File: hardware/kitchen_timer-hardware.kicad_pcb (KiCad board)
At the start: 2 copper layers, 60 x 110.8 mm, 80 parts, among them J1 Conn_01x02, J2 Conn_01x02_Pin, J3 AVR-ISP-6, Q1 JSM2302, Q2 IRLML6402, Q3 MMBT3904, SW2 SKRPACE010, U1 CH340E UART Module, U10 MAX7219, U11 KWM-20882CUYB, U12 KWM-20882CUYB, U13 KWM-20882CUYB, U14 KWM-20882CUYB, U2 TP4056 breakout, U3 SparkFun_LiPower, U5 ATMEGA328P-AU, U6 PEC11R-4215F-S0024, U7 MAX7219, U8 MAX7219, U9 MAX7219, Y1 Crystal-32kHz

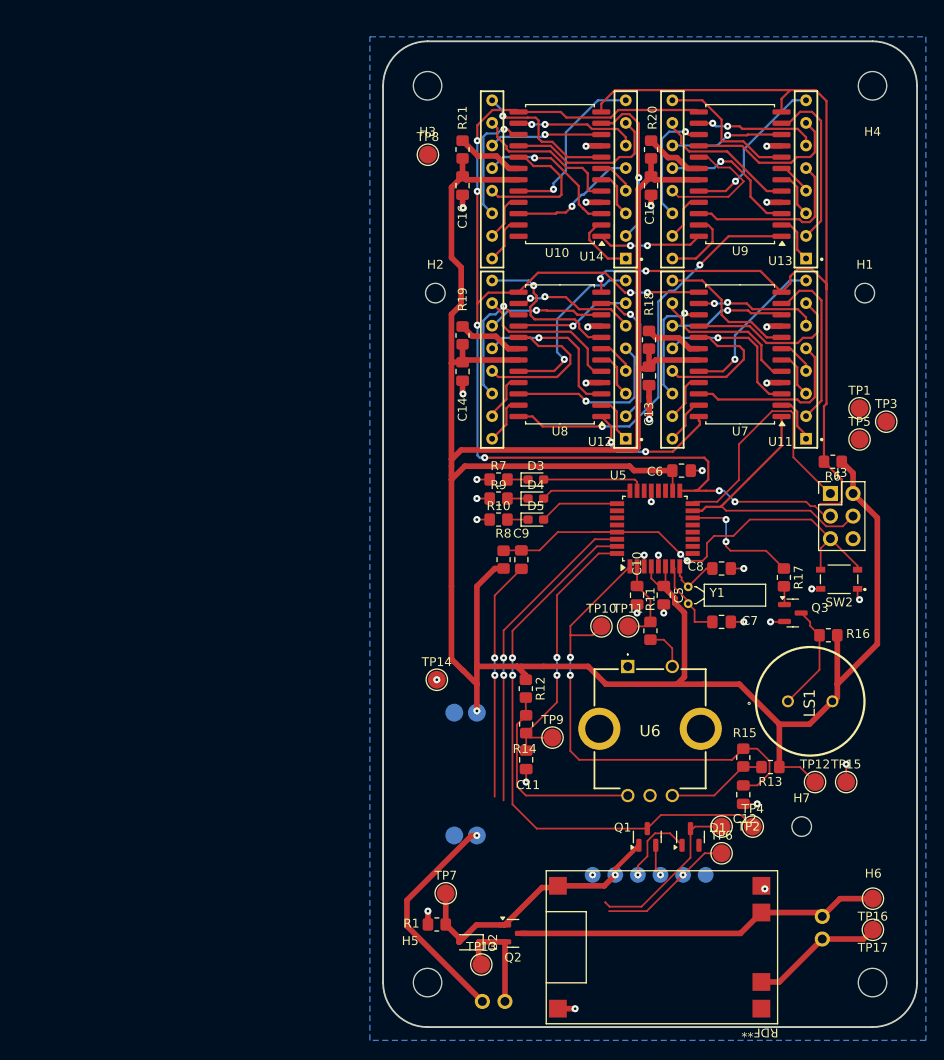
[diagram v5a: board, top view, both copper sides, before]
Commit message: Search/replace via size to adhere to JLCPCB fabrication rules
Down from 130 to 85 DRC rules now
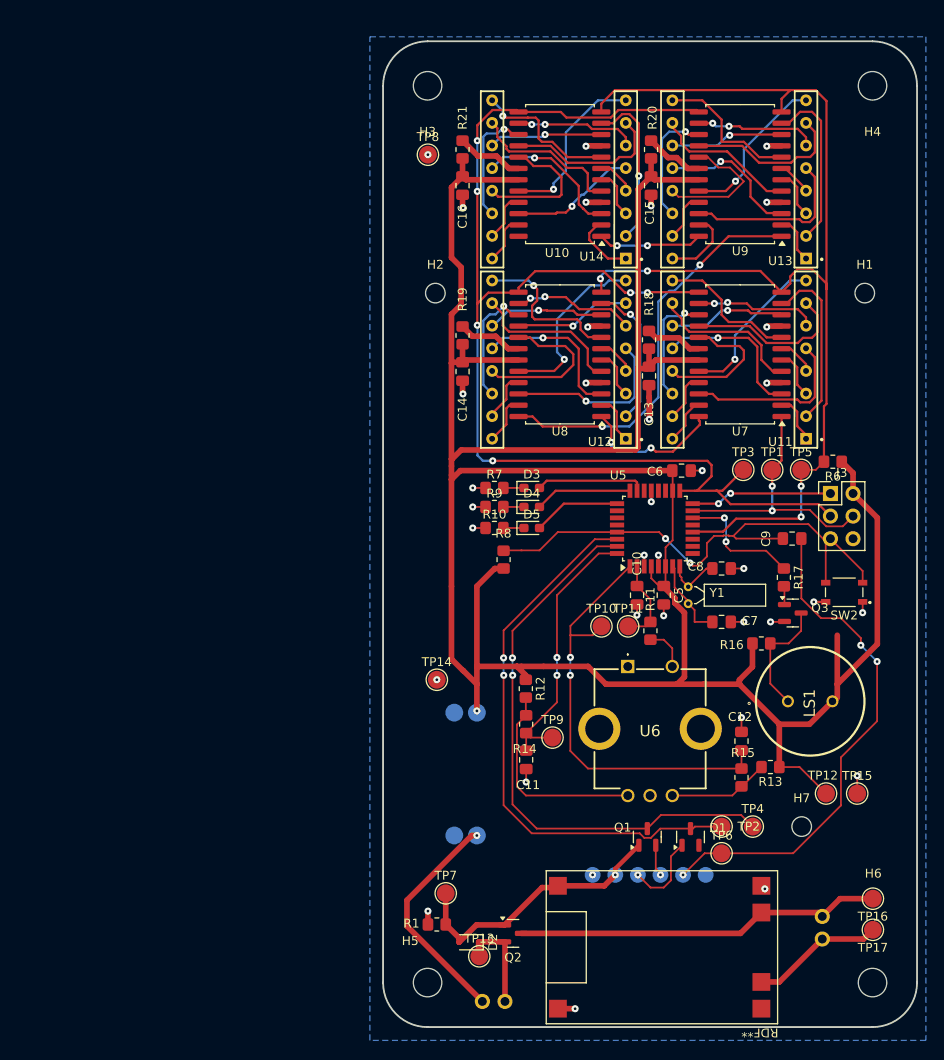
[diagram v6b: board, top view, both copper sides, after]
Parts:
- moved C9 30.5 mm to (173.0, 83.8), turned to 180 degrees
- moved TP3 17.0 mm to (167.5, 76.1)
- moved TP1 12.0 mm to (170.7, 76.1)
- moved R16 7.59 mm to (169.5, 95.6), turned to 180 degrees
- moved TP5 7.40 mm to (174.0, 76.1)
- moved C12 6.02 mm to (167.3, 106.6), turned to 90 degrees
- moved R15 2.24 mm to (167.3, 110.7)
- moved TP12 1.79 mm to (176.8, 112.5)
- moved TP15 1.79 mm to (180.3, 112.5)
- moved SW2 1.57 mm to (178.8, 89.9)
- moved R10 1.05 mm to (139.5, 82.6)
- moved R7 1.05 mm to (139.5, 78.1)
- moved R9 1.05 mm to (139.5, 80.3)
- moved D3 1.05 mm to (143.7, 78.1)
- moved D4 1.05 mm to (143.7, 80.3)
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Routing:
- net +5V: track 302.4 -> 317.8 mm
- net /Microcontroller/DTR: track 43.1 -> 57.5 mm
- net /LED Matrices Drivers/CS: track 110.0 -> 123.3 mm, vias 2 -> 4
- net /Microcontroller/MISO: track 29.0 -> 16.0 mm, vias 0 -> 2
- net /Microcontroller/MCU_RXD: track 55.3 -> 63.4 mm
- net /Microcontroller/ENCODER_CH_B: track 56.2 -> 49.5 mm
- net /Microcontroller/RESET: track 54.6 -> 60.0 mm
- net /LED Matrices Drivers/SCK: track 139.1 -> 144.3 mm, vias 8 -> 6
- net /LED Matrices Drivers/MOSI: track 33.1 -> 30.5 mm, vias 0 -> 2
- net Net-(Q3-C): track 12.2 -> 13.4 mm
- net /+5V Boost Converter/PP_VCC: track 12.3 -> 11.3 mm
- net /Microcontroller/TEST_LED3: track 8.99 -> 9.85 mm
- net /Microcontroller/TEST_LED2: track 10.1 -> 10.9 mm
- net GND: track 48.1 -> 49.0 mm, vias 33 -> 34
- net /LED Matrices Drivers/Mat1B.SEG_G: track 17.3 -> 18.1 mm
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
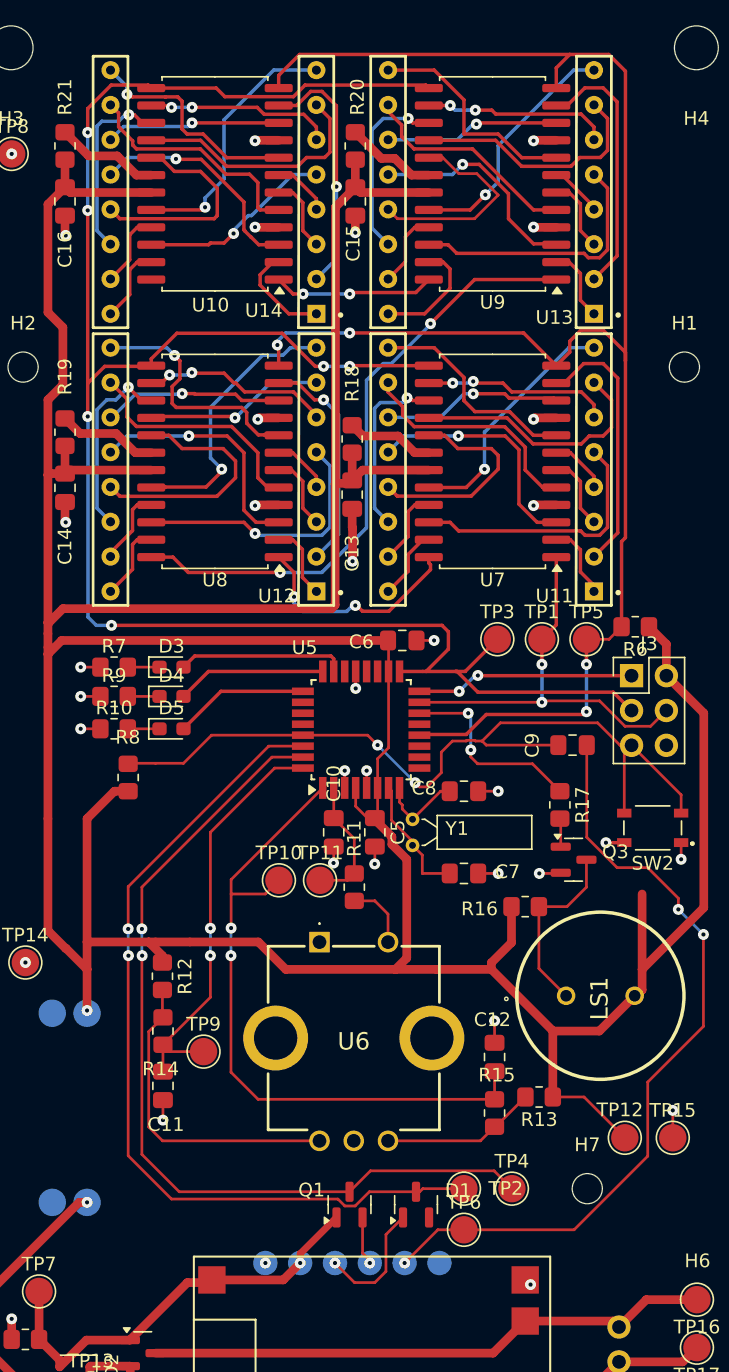
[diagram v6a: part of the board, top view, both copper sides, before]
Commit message: Fix all DRC errors relating to vias and traces
Still 49 errors regarding footprints and silkscreen
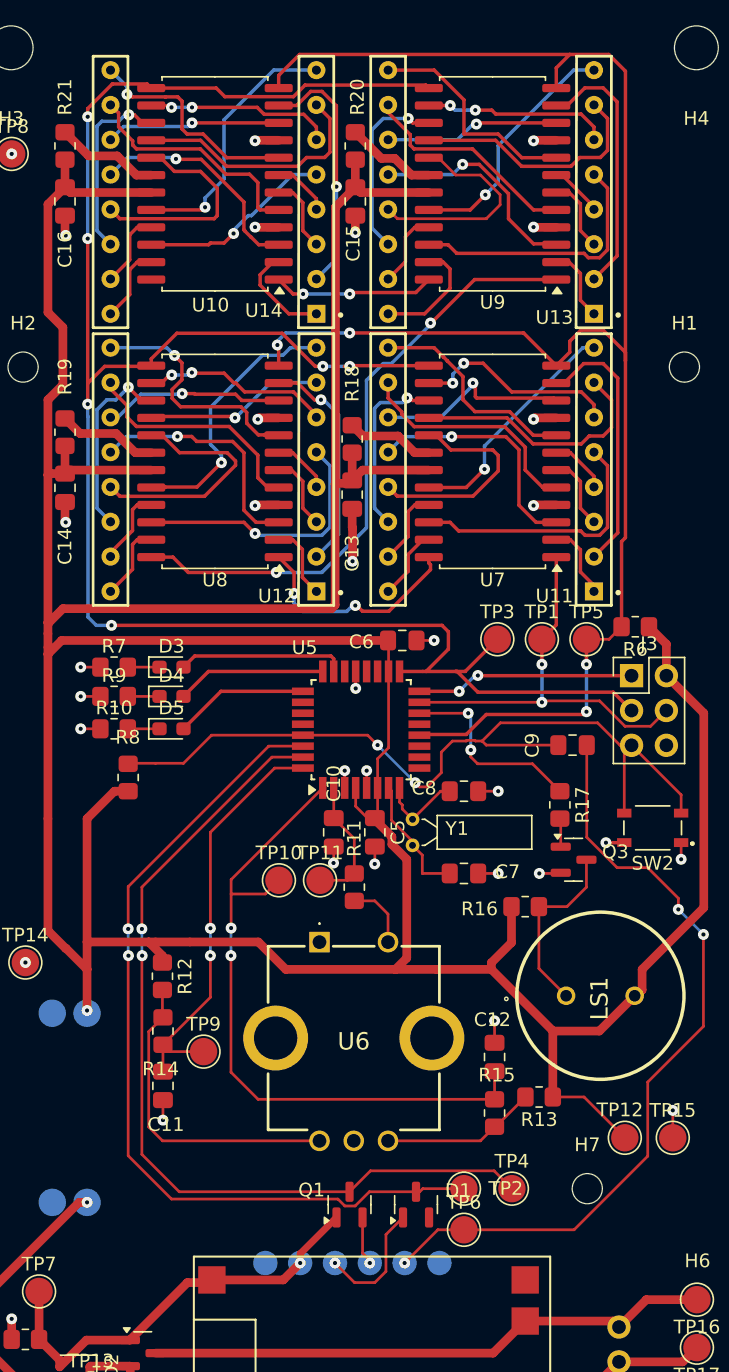
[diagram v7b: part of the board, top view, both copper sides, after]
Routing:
- net +5V: track 317.8 -> 312.3 mm
- net /LED Matrices Drivers/Mat1A.SEG_A: track 13.7 -> 15.2 mm
- net /LED Matrices Drivers/Mat1A.DIG_5: track 13.2 -> 14.4 mm
- net /LED Matrices Drivers/Mat2A.SEG_G: track 15.2 -> 15.9 mm
- net /LED Matrices Drivers/Mat1A.SEG_G: track 15.8 -> 16.4 mm
- net /LED Matrices Drivers/Mat1A.SEG_C: track 17.9 -> 17.3 mm
- net /LED Matrices Drivers/Mat1B.SEG_G: track 18.1 -> 17.6 mm
- net unconnected-(U2-OUT+-Pad3): vias 1 -> 0
- net GND: vias 34 -> 33
